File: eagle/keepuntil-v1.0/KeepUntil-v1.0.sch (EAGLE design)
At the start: 24 parts, among them IC2 REG1117, Q1 CSTCR6M00G53Z, T1 BC846, U1 ATMEGA328P-AU, X1 MINI-USB-32005-201

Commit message: schematic
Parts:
- added S1: SWITCH-MOMENTARY-2SMD-1101NE, SparkFun-Electromechanical:SWITCH-MOMENTARY-2SMD-1101NE
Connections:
- net GND: now also S1.1
- net RESET: now also S1.2
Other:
- moved on the sheet: R1
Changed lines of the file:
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@@
 <part name="KEYPAD" library="adafruit" deviceset="PINHD-2X4" device=""/>
 <part name="CONTROL" library="pinhead" deviceset="PINHD-2X5" device=""/>
+<part name="S1" library="SparkFun-Electromechanical" deviceset="SWITCH-MOMENTARY-2" device="SMD-1101NE"/>
+<part name="GND9" library="supply1" deviceset="GND" device=""/>
 </parts>
 <sheets>
@@
 </instance>
 <instance part="U1" gate="A" x="180.34" y="86.36"/>
-<instance part="R1" gate="G$1" x="223.52" y="109.22" rot="R90"/>
+<instance part="R1" gate="G$1" x="228.6" y="109.22" rot="R90"/>
 <instance part="C2" gate="G$1" x="99.06" y="142.24"/>
 <instance part="C4" gate="G$1" x="66.04" y="142.24"/>
@@
 <instance part="R2" gate="G$1" x="104.14" y="40.64" rot="R180"/>
 <instance part="RTC" gate="A" x="86.36" y="104.14"/>
-<instance part="P+2" gate="VCC" x="223.52" y="121.92"/>
+<instance part="P+2" gate="VCC" x="228.6" y="121.92"/>
 <instance part="P+3" gate="VCC" x="157.48" y="121.92"/>
 <instance part="P+6" gate="VCC" x="66.04" y="35.56"/>
@@
 <attribute name="VALUE" x="24.13" y="30.48" size="1.778" layer="96" rot="R180"/>
 </instance>
+<instance part="S1" gate="G$1" x="228.6" y="83.82" smashed="yes" rot="R90">
+<attribute name="NAME" x="226.06" y="81.28" size="1.778" layer="95" rot="R90"/>
+</instance>
+<instance part="GND9" gate="1" x="228.6" y="76.2"/>
 </instances>
 <busses>
@@
 <segment>
 <pinref part="U1" gate="A" pin="PC6"/>
-<wire x1="198.12" y1="93.98" x2="223.52" y2="93.98" width="0.1524" layer="91"/>
+<wire x1="198.12" y1="93.98" x2="228.6" y2="93.98" width="0.1524" layer="91"/>
 <pinref part="R1" gate="G$1" pin="1"/>
-<wire x1="223.52" y1="104.14" x2="223.52" y2="101.6" width="0.1524" layer="91"/>
-<wire x1="223.52" y1="101.6" x2="223.52" y2="93.98" width="0.1524" layer="91"/>
-<wire x1="223.52" y1="101.6" x2="228.6" y2="101.6" width="0.1524" layer="91"/>
-<label x="228.6" y="101.6" size="1.27" layer="95" xref="yes"/>
-<junction x="223.52" y="101.6"/>
+<wire x1="228.6" y1="104.14" x2="228.6" y2="101.6" width="0.1524" layer="91"/>
+<wire x1="228.6" y1="101.6" x2="228.6" y2="93.98" width="0.1524" layer="91"/>
+<wire x1="228.6" y1="101.6" x2="233.68" y2="101.6" width="0.1524" layer="91"/>
+<label x="233.68" y="101.6" size="1.27" layer="95" xref="yes"/>
+<junction x="228.6" y="101.6"/>
+<pinref part="S1" gate="G$1" pin="2"/>
+<wire x1="228.6" y1="93.98" x2="228.6" y2="88.9" width="0.1524" layer="91"/>
+<junction x="228.6" y="93.98"/>
 </segment>
 <segment>
@@
 <segment>
 <pinref part="R1" gate="G$1" pin="2"/>
-<wire x1="223.52" y1="114.3" x2="223.52" y2="119.38" width="0.1524" layer="91"/>
+<wire x1="228.6" y1="114.3" x2="228.6" y2="119.38" width="0.1524" layer="91"/>
 <pinref part="P+2" gate="VCC" pin="VCC"/>
 </segment>
@@
 <pinref part="GND3" gate="1" pin="GND"/>
 </segment>
-</net>
+<segment>
+<pinref part="S1" gate="G$1" pin="1"/>
+<pinref part="GND9" gate="1" pin="GND"/>
+</segment>
+</net>

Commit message: schematic
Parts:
- removed CONTROL: (no value), pinhead:PINHD-2X5
- removed KEYPAD: (no value), adafruit:PINHD-2X4
- removed LOCK-CTRL: (no value), pinhead:PINHD-2X4
- removed RTC: (no value), pinhead:PINHD-2X2
- removed SERIAL: (no value), adafruit:PINHD-1X3
- added JP1: (no value), pinhead:PINHD-2X6
- added JP2: (no value), pinhead:PINHD-2X4
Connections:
- removed net LED-GRN: LOCK-CTRL.7
- removed net LED-RED: LOCK-CTRL.8
- removed net SERVO: LOCK-CTRL.1
- new net COL1: JP2.1
- new net COL2: JP2.3
- new net COL3: JP2.5
- new net N$15: R3.2
- new net N$16: R4.1
- new net N$17: R4.2
- new net N$18: R5.1
- new net N$19: R6.1
- new net N$22: R5.2
- new net N$23: R6.2
- new net N$5: R3.1
- new net ROW1: JP2.2, R9.1
- new net ROW2: JP2.4, R8.1, R9.2
- new net ROW3: JP2.6, R8.2
- net GND: no longer LOCK-CTRL.5, RTC.4, SERIAL.3
- net RTC-SCL: no longer RTC.3
- net RTC-SDA: no longer RTC.1
- net RX: no longer SERIAL.1
- net SOLENOID: no longer LOCK-CTRL.2
- net TX: no longer SERIAL.2
- net VCC: no longer LOCK-CTRL.3, LOCK-CTRL.4, RTC.2
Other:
- moved on the sheet: R3, R4

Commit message: schematic & board
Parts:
- removed JP2: (no value), pinhead:PINHD-2X4
- added KEYPAD: (no value), pinhead:PINHD-2X4
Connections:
- removed net COL1: JP2.1
- removed net N$14: U1.PC3
- removed net N$15: R3.2
- removed net N$16: R4.1
- removed net N$17: R4.2
- removed net N$18: R5.1
- removed net N$19: R6.1
- removed net N$22: R5.2
- removed net N$23: R6.2
- removed net N$5: R3.1
- removed net ROW1: JP2.2, R9.1
- new net KEYPAD: KEYPAD.1, R3.2, R4.2, U1.PC3
- new net ROW4: KEYPAD.8, R6.2
- net COL2: now also KEYPAD.3, R4.1, R5.2; no longer JP2.3
- net COL3: now also KEYPAD.5, R5.1; no longer JP2.5
- net GND: now also R3.1
- net ROW2: now also KEYPAD.4; no longer JP2.4
- net ROW3: now also KEYPAD.6, R6.1; no longer JP2.6
- net VCC: now also KEYPAD.2, R9.1
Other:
- moved on the sheet: R3, R4, R5, R6, R8

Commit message: schematic
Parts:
- removed R3, R4, R5: 1K, resistor:R-EU_R0805
- removed R6, R8, R9: 4.7K, resistor:R-EU_R0805
- added JP2: (no value), pinhead:PINHD-1X3
- JP1: device pinhead:PINHD-2X6 -> pinhead:PINHD-2X11
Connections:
- net RTC-SCL renamed SCL
- net RTC-SDA renamed SDA
- removed net KEYPAD: KEYPAD.1, R3.2, R4.2, U1.PC3
- new net COL1: KEYPAD.1
- new net N$14: U1.PC1
- new net N$15: U1.PC2
- new net N$16: U1.PC3
- new net N$5: U1.PC0
- new net ROW1: KEYPAD.2
- net COL2: no longer R4.1, R5.2
- net COL3: no longer R5.1
- net GND: now also Q1.2; no longer R3.1
- net ROW2: no longer R8.1, R9.2
- net ROW3: no longer R6.1, R8.2
- net ROW4: no longer R6.2
- net VCC: no longer KEYPAD.2, R9.1
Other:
- moved on the sheet: KEYPAD, R2, T1

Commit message: Schematic
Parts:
- removed JP2: (no value), pinhead:PINHD-1X3
- removed X1: MINI-USB-32005-201, con-cypressindustries:MINI-USB-32005-201
- added C1: 0.1uF, resistor:C-EUC0805
- added J1: USB-MICROB, SparkFun-Connectors:USB-MICROB
- added SERIAL: (no value), pinhead:PINHD-1X6
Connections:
- new net N$17: C1.2, SERIAL.6
- net GND: now also J1.GND, SERIAL.1; no longer X1.5
- net N$4: now also J1.VBUS; no longer X1.1
- net RESET: now also C1.1
- net RX: now also SERIAL.4
- net TX: now also SERIAL.5
- net VCC: now also SERIAL.3
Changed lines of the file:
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@@
 <part name="C4" library="resistor" deviceset="C-EU" device="C0805" value="0.1uF"/>
 <part name="C5" library="resistor" deviceset="C-EU" device="C0805" value="0.1uF"/>
-<part name="X1" library="con-cypressindustries" deviceset="MINI-USB-" device="32005-201"/>
 <part name="FRAME1" library="frames" deviceset="A4L-LOC" device=""/>
 <part name="LED1" library="led" deviceset="LED" device="SMT1206"/>
@@
 <part name="GND3" library="supply1" deviceset="GND" device=""/>
 <part name="JP1" library="pinhead" deviceset="PINHD-2X11" device=""/>
-<part name="JP2" library="pinhead" deviceset="PINHD-1X3" device=""/>
+<part name="SERIAL" library="pinhead" deviceset="PINHD-1X6" device=""/>
+<part name="C1" library="resistor" deviceset="C-EU" device="C0805" value="0.1uF"/>
+<part name="J1" library="SparkFun-Connectors" deviceset="USB" device="-MICROB"/>
 </parts>
 <sheets>
@@
 <instance part="C4" gate="G$1" x="66.04" y="142.24"/>
 <instance part="C5" gate="G$1" x="124.46" y="86.36"/>
-<instance part="X1" gate="G$1" x="30.48" y="142.24" smashed="yes" rot="MR0"/>
 <instance part="FRAME1" gate="G$1" x="0" y="0"/>
 <instance part="LED1" gate="G$1" x="111.76" y="132.08"/>
@@
 <instance part="GND7" gate="1" x="66.04" y="15.24"/>
 <instance part="GND10" gate="1" x="213.36" y="142.24"/>
-<instance part="GND11" gate="1" x="38.1" y="129.54"/>
-<instance part="GND8" gate="1" x="17.78" y="78.74"/>
+<instance part="GND11" gate="1" x="30.48" y="137.16"/>
+<instance part="GND8" gate="1" x="172.72" y="137.16"/>
 <instance part="P+4" gate="VCC" x="17.78" y="86.36"/>
-<instance part="P+5" gate="VCC" x="25.4" y="86.36"/>
+<instance part="P+5" gate="VCC" x="182.88" y="149.86" rot="R270"/>
 <instance part="IC2" gate="G$1" x="83.82" y="147.32" smashed="yes"/>
 <instance part="P+1" gate="VCC" x="121.92" y="147.32" rot="R270"/>
@@
 <instance part="GND3" gate="1" x="124.46" y="53.34"/>
 <instance part="JP1" gate="A" x="81.28" y="88.9"/>
-<instance part="JP2" gate="A" x="88.9" y="35.56"/>
+<instance part="SERIAL" gate="A" x="160.02" y="152.4" smashed="yes" rot="R180">
+<attribute name="NAME" x="166.624" y="162.687" size="1.778" layer="95" rot="R180"/>
+<attribute name="VALUE" x="166.37" y="162.56" size="1.778" layer="96" rot="R180"/>
+</instance>
+<instance part="C1" gate="G$1" x="180.34" y="157.48" smashed="yes" rot="R270">
+<attribute name="NAME" x="180.975" y="161.29" size="1.778" layer="95" rot="R270"/>
+<attribute name="VALUE" x="175.641" y="164.846" size="1.778" layer="96" rot="R270"/>
+</instance>
+<instance part="J1" gate="G$1" x="25.4" y="144.78" rot="MR0"/>
 </instances>
 <busses>
@@
 <label x="66.04" y="25.4" size="1.27" layer="95" xref="yes"/>
 </segment>
+<segment>
+<pinref part="C1" gate="G$1" pin="1"/>
+<wire x1="182.88" y1="157.48" x2="185.42" y2="157.48" width="0.1524" layer="91"/>
+<label x="185.42" y="157.48" size="1.27" layer="95" rot="MR180" xref="yes"/>
+</segment>
 </net>
 <net name="N$7" class="0">
@@
 <label x="203.2" y="86.36" size="1.27" layer="95" xref="yes"/>
 </segment>
+<segment>
+<pinref part="SERIAL" gate="A" pin="5"/>
+<wire x1="162.56" y1="154.94" x2="170.18" y2="154.94" width="0.1524" layer="91"/>
+<label x="170.18" y="154.94" size="1.27" layer="95" rot="MR180" xref="yes"/>
+</segment>
 </net>
 <net name="RX" class="0">
@@
 <wire x1="198.12" y1="88.9" x2="203.2" y2="88.9" width="0.1524" layer="91"/>
 <label x="203.2" y="88.9" size="1.27" layer="95" xref="yes"/>
+</segment>
+<segment>
+<pinref part="SERIAL" gate="A" pin="4"/>
+<wire x1="162.56" y1="152.4" x2="170.18" y2="152.4" width="0.1524" layer="91"/>
+<label x="170.18" y="152.4" size="1.27" layer="95" rot="MR180" xref="yes"/>
 </segment>
 </net>
@@
 <junction x="111.76" y="147.32"/>
 </segment>
+<segment>
+<pinref part="SERIAL" gate="A" pin="3"/>
+<pinref part="P+5" gate="VCC" pin="VCC"/>
+<wire x1="162.56" y1="149.86" x2="180.34" y2="149.86" width="0.1524" layer="91"/>
+</segment>
 </net>
 <net name="GND" class="0">
@@
 </segment>
 <segment>
-<pinref part="X1" gate="G$1" pin="5"/>
-<wire x1="35.56" y1="137.16" x2="38.1" y2="137.16" width="0.1524" layer="91"/>
-<wire x1="38.1" y1="137.16" x2="38.1" y2="132.08" width="0.1524" layer="91"/>
-<pinref part="GND11" gate="1" pin="GND"/>
-</segment>
-<segment>
 <pinref part="S1" gate="G$1" pin="1"/>
 <pinref part="GND9" gate="1" pin="GND"/>
@@
 <pinref part="GND3" gate="1" pin="GND"/>
 </segment>
+<segment>
+<pinref part="SERIAL" gate="A" pin="1"/>
+<pinref part="GND8" gate="1" pin="GND"/>
+<wire x1="162.56" y1="144.78" x2="172.72" y2="144.78" width="0.1524" layer="91"/>
+<wire x1="172.72" y1="144.78" x2="172.72" y2="139.7" width="0.1524" layer="91"/>
+</segment>
+<segment>
+<pinref part="J1" gate="G$1" pin="GND"/>
+<pinref part="GND11" gate="1" pin="GND"/>
+<wire x1="27.94" y1="144.78" x2="30.48" y2="144.78" width="0.1524" layer="91"/>
+<wire x1="30.48" y1="144.78" x2="30.48" y2="139.7" width="0.1524" layer="91"/>
+</segment>
 </net>
 <net name="N$4" class="0">
 <segment>
 <pinref part="IC2" gate="G$1" pin="VIN"/>
-<pinref part="X1" gate="G$1" pin="1"/>
 <wire x1="71.12" y1="147.32" x2="66.04" y2="147.32" width="0.1524" layer="91"/>
 <pinref part="C4" gate="G$1" pin="1"/>
-<wire x1="66.04" y1="147.32" x2="35.56" y2="147.32" width="0.1524" layer="91"/>
+<wire x1="66.04" y1="147.32" x2="27.94" y2="147.32" width="0.1524" layer="91"/>
 <wire x1="66.04" y1="147.32" x2="66.04" y2="144.78" width="0.1524" layer="91"/>
 <junction x="66.04" y="147.32"/>
+<pinref part="J1" gate="G$1" pin="VBUS"/>
 </segment>
 </net>
@@
 </segment>
 </net>
+<net name="N$17" class="0">
+<segment>
+<pinref part="SERIAL" gate="A" pin="6"/>
+<wire x1="162.56" y1="157.48" x2="175.26" y2="157.48" width="0.1524" layer="91"/>
+<pinref part="C1" gate="G$1" pin="2"/>
+</segment>
+</net>

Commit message: schematic
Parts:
- removed JP1: (no value), pinhead:PINHD-2X11
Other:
- moved on the sheet: C2, C4, C5, ISP, J1, KEYPAD, LED1, Q1, R1, R2, R7, S1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

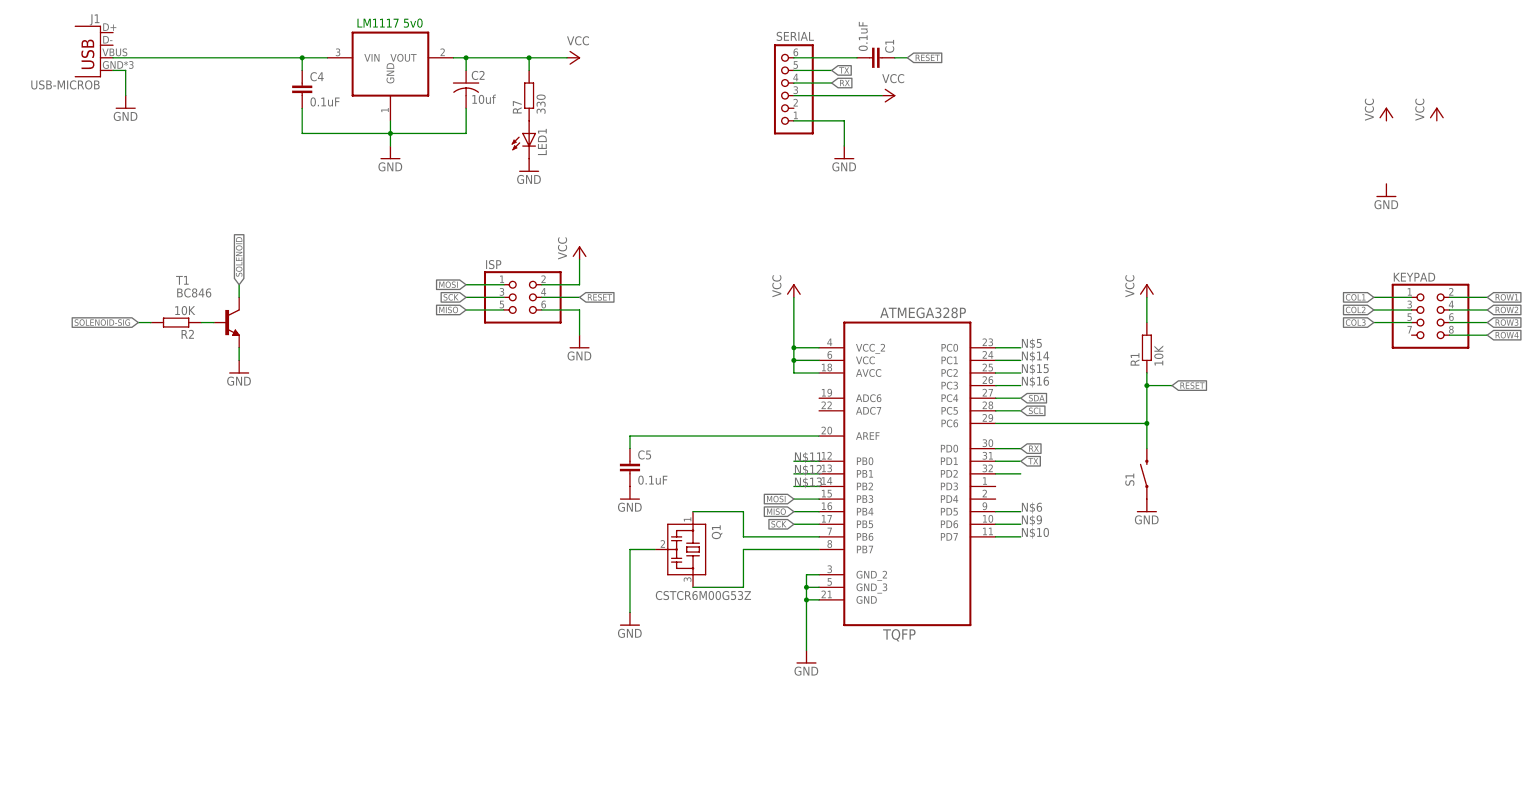
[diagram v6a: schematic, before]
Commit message: schematic cleanup and board
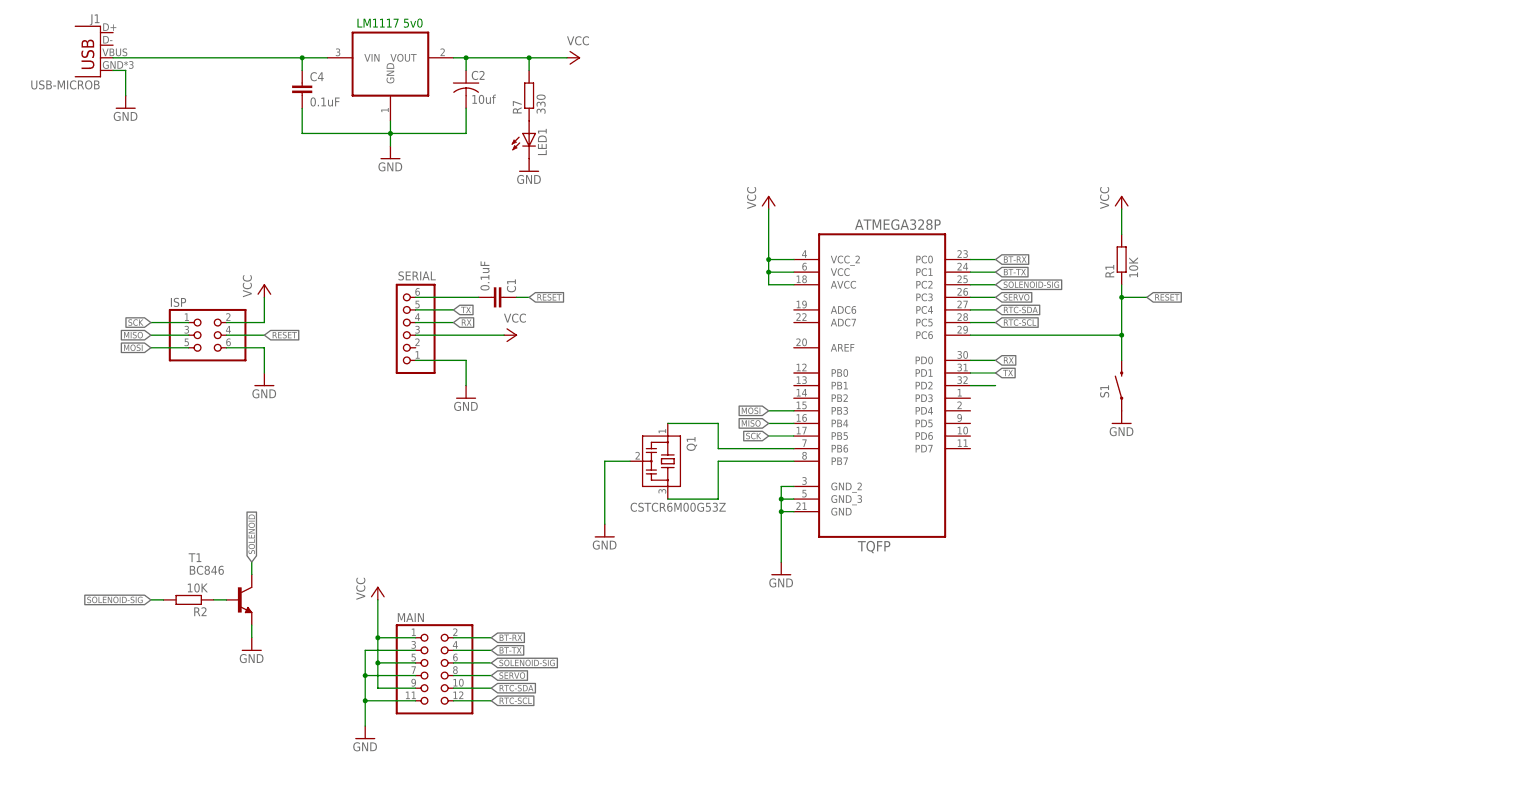
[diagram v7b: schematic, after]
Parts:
- removed C5: 0.1uF, resistor:C-EUC0805
- removed KEYPAD: (no value), pinhead:PINHD-2X4
- added MAIN: (no value), pinhead:PINHD-2X6
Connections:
- removed net COL1: KEYPAD.1
- removed net COL2: KEYPAD.3
- removed net COL3: KEYPAD.5
- removed net N$10: U1.PD7
- removed net N$11: U1.PB0
- removed net N$12: U1.PB1
- removed net N$13: U1.PB2
- removed net N$14: U1.PC1
- removed net N$15: U1.PC2
- removed net N$16: U1.PC3
- removed net N$5: U1.PC0
- removed net N$6: U1.PD5
- removed net N$8: C5.1, U1.AREF
- removed net N$9: U1.PD6
- removed net ROW1: KEYPAD.2
- removed net ROW2: KEYPAD.4
- removed net ROW3: KEYPAD.6
- removed net ROW4: KEYPAD.8
- removed net SCL: U1.PC5
- removed net SDA: U1.PC4
- new net BT-RX: MAIN.2, U1.PC0
- new net BT-TX: MAIN.4, U1.PC1
- new net RTC-SCL: MAIN.12, U1.PC5
- new net RTC-SDA: MAIN.10, U1.PC4
- new net SERVO: MAIN.8, U1.PC3
- net GND: now also MAIN.11, MAIN.3, MAIN.7; no longer C5.2
- net MISO: now also ISP.3; no longer ISP.5
- net MOSI: now also ISP.5; no longer ISP.1
- net SCK: now also ISP.1; no longer ISP.3
- net SOLENOID-SIG: now also MAIN.6, U1.PC2
- net VCC: now also MAIN.1, MAIN.5, MAIN.9
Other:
- moved on the sheet: C1, ISP, Q1, R1, R2, S1, SERIAL, T1
